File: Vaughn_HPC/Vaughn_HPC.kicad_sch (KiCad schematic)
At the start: 24 parts, among them U1 LM7805_TO220, U2 LM7812_TO220

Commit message: WIP
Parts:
- added J1: Conn_01x06_Pin, symbol Connector:Conn_01x06_Pin
- added R1, R2, R3, R4, R5, R6: R, symbol Device:R
- added R7: 1M, symbol Device:R
- added R8, R9: 1K, symbol Device:R
- added U3: PIC16LF1938-I/SP, SPDIP28_300MC_MCH, symbol PIC16LF1933:PIC16LF1938-I_SP
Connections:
- net at TR1.1: now also RV1.1
- net at TR1.4: now also RV1.2
- net at TR1.5: now also D3.2 (A), D4.1 (K), TR1.7
- net at TR1.6: now also D1.1 (K), D2.2 (A), TR1.8
- net at C2.1: now also U2.3 (VO)
- net GND: now reaches C2.2
- net GND: now also C1.2, C3.2, C4.2, D1.2 (A), D4.2 (A), U1.2 (GND), U2.2 (GND), R1.2, R2.2, R3.2, R4.1, R5.2, R6.1, U3.19 (VSS), U3.8 (VSS)
- net at U1.3 (VO): now also C3.1
- net at C1.1: now also D2.1 (K), D3.1 (K)
- net at C4.1: now also U3.20 (VDD)
- new net: R3.1, U3.2 (RA0)
- new net: R4.2, U3.3 (RA1)
- new net: R2.1, U3.5 (RA3)
- new net: R1.1, U3.21 (RB0)
- new net: R9.1, U3.12 (RC1)
- new net: R5.1, U3.24 (RB3)
- new net: R6.2, U3.4 (RA2), U3.7 (RA5)
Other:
- moved on the sheet: C1, C2, C3, C4, D1, D2, D3, D4, RN1, RN2, TP1, TP10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

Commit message: Add files via upload
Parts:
- removed TP1, TP10, TP2, TP3, TP4, TP5, TP6, TP7, TP8, TP9: TestPoint, symbol Connector:TestPoint
- added D5, D6, D7, D9: 1N4001, Diode_THT:D_DO-41_SOD81_P10.16mm_Horizontal, symbol Diode:1N4001
- added J2, J3, J4: AZ943-1CH-24DE, AZ9431CH24DE, symbol sugar:AZ943-1CH-24DE
- added K1: AZ2100-1A-12DEF, AZ21001A12DEF, symbol cubey:AZ2100-1A-12DEF
- added Q1, Q2, Q3, Q5: 2N3904, Package_TO_SOT_THT:TO-92_Inline, symbol Transistor_BJT:2N3904
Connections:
- net at C2.1, U2.3 (VO): now also U1.1 (VI)
- net at U2.1 (VI): now also C1.1, D2.1 (K), D3.1 (K)
- new net: D9.1 (K), K1.3 (COIL_2)
- new net: D9.2 (A), K1.2 (COIL_1)
- new net: D6.2 (A), J3.2 (COIL_1)
- new net: D6.1 (K), J3.5 (COIL_2)
- new net: D5.2 (A), J2.2 (COIL_1)
- new net: D5.1 (K), J2.5 (COIL_2)
- new net: D7.2 (A), J4.2 (COIL_1)
- new net: D7.1 (K), J4.5 (COIL_2)
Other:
- moved on the sheet: C1, C2, C3, J1, U1, U2

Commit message: Add files via upload
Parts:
- added J10, J11, J12, J13, J14, J15, J16, J17, J5, J8, J9: 1287, 1287:KEYSTONE_1287, symbol spade2:1287
- added J6, J7: 1267, 1267:KEYSTONE_1267, symbol spade:1267
- renumbered Q5 to Q4
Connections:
- net GND: now also Q1.1 (E), Q2.1 (E), Q3.1 (E), Q4.1 (E)
- net at RV1.1, TR1.1: now also J16.1_1
- net at RV1.2, TR1.4: now also J17.1_2
- net at J3.1 (COM): now also J11.1_2
- net at J3.3 (NO): now also J12.1_1
- net at J3.4 (NC): now also J10.1_2
- net 12V: now reaches D6.1 (K), J3.5 (COIL_2)
- net 12V: now also C2.1, D5.1 (K), D7.1 (K), J2.5 (COIL_2), J4.5 (COIL_2), U1.1 (VI), U2.3 (VO)
- net at J2.1 (COM): now also J8.1_2
- net at J2.3 (NO): now also J9.1_1
- net at J2.4 (NC): now also J5.1_2
- net 5V: now reaches C3.1, U1.3 (VO)
- net at J4.1 (COM): now also J13.1_2
- net at J4.3 (NO): now also J15.1_1
- net at J4.4 (NC): now also J14.1_2
- net at K1.1 (COM): now also J6.1
- net at K1.4 (NO): now also J7.1
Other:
- moved on the sheet: C1, C2, C3, C4, D1, D2, D3, D4, D5, D6, D7, D9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

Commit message: Update Vaughn_HPC.kicad_sch
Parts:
- R9: value 1K -> 120
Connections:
- net GND: now also J1.4 (Pin_4)
- net at D6.2 (A), J3.2 (COIL_1): now also Q2.3 (C)
- net at Q3.3 (C): now also D7.2 (A), J4.2 (COIL_1)
- net at D5.2 (A), J2.2 (COIL_1): now also Q1.3 (C)
- net prog_p2: now reaches J1.2 (Pin_2)
- net prog_p2: now also U3.27 (RB6/ICSPCLK/ICDCLK)
- net at J1.5 (Pin_5): now also R7.1
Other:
- moved on the sheet: Q1, Q2, Q3, R7

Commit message: updated Traces
Bom
not done, but very close.
missing a couple connectors, and the specific mosfets
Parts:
- added J12, J13, J14, J15, J16: 1825640000, CONN4_1825640000_WED, symbol quickConnect:1825640000
- renumbered Q4 to Q1, Q1 to Q4
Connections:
- net GND: now also J16.4; no longer Q1.1 (E)
- net RP2_3_q1_Emitter: now reaches RN2.3 (R2)
- net RP2_3_q1_Emitter: now also Q1.1 (E)
- net at D9.2 (A), K1.2 (COIL_1): now also Q1.3 (C)
- net RP1_4_q3_base: now reaches Q3.2 (B)
- net RP1_4_q3_base: now also RN1.4 (R3)
- net RP1_6_q4_base: now reaches Q4.2 (B)
- net RP1_6_q4_base: now also RN1.6 (R5)
- net prog1_j14: now reaches J1.1 (Pin_1)
- net prog1_j14: now also J14.1
- net prog3_mcu28: now reaches J1.3 (Pin_3)
- net prog3_mcu28: now also U3.28 (RB7/ICSPDAT/ICDDAT)
- net prog6_mcu1: now reaches J1.6 (Pin_6)
- net prog6_mcu1: now also U3.1 (VPP/*MCLR/RE3)
- net mcu11_j16: now reaches U3.11 (RC0)
- net mcu11_j16: now also J16.1
- net RP1_1_mcu6: now reaches U3.6 (RA4)
- net mcu9_array1: now reaches U3.9 (RA7)
- net mcu9_array1: now also RN1.1 (common)
- net RP1_2_Q2_base: now reaches Q2.2 (B)
- net RP1_2_Q2_base: now also RN1.2 (R1)
- net RP1_8_q1_base: now reaches RN1.8 (R7)
- net prog_p2 renamed prog2_mcu27
- new net: J12.1, J13.4, J14.4, J15.4
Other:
- moved on the sheet: Q1

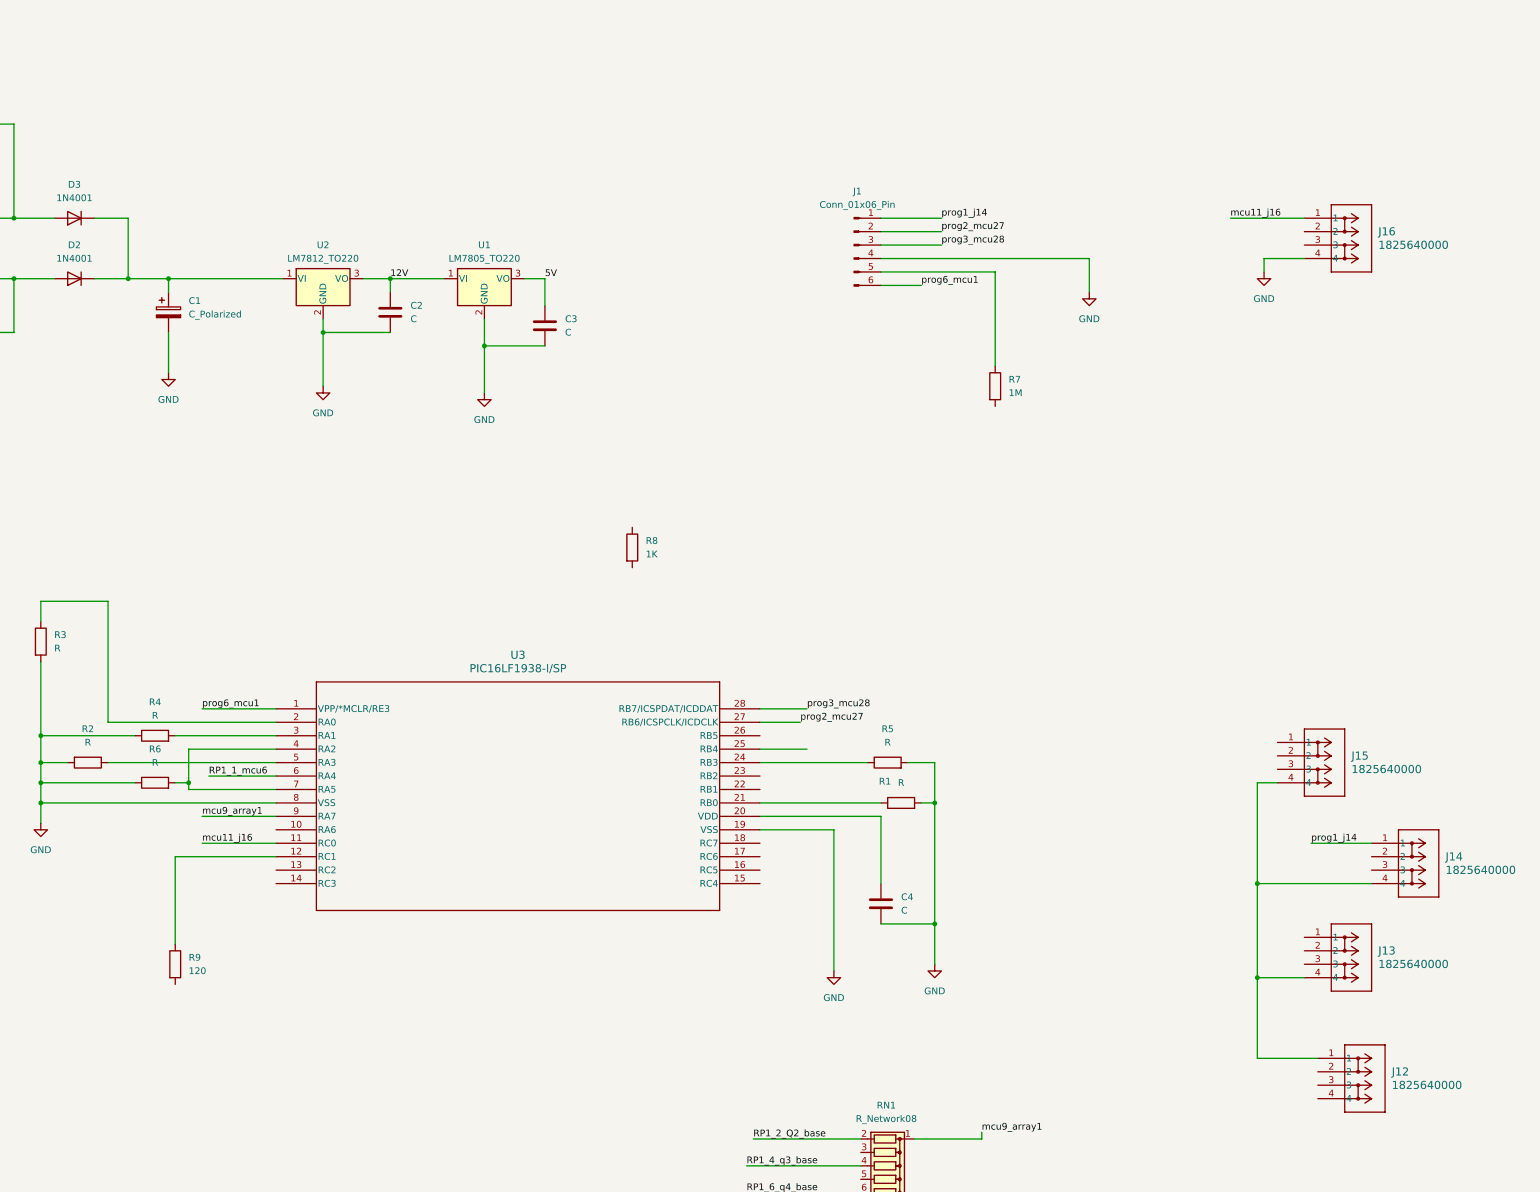
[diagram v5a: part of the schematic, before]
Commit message: add the LED
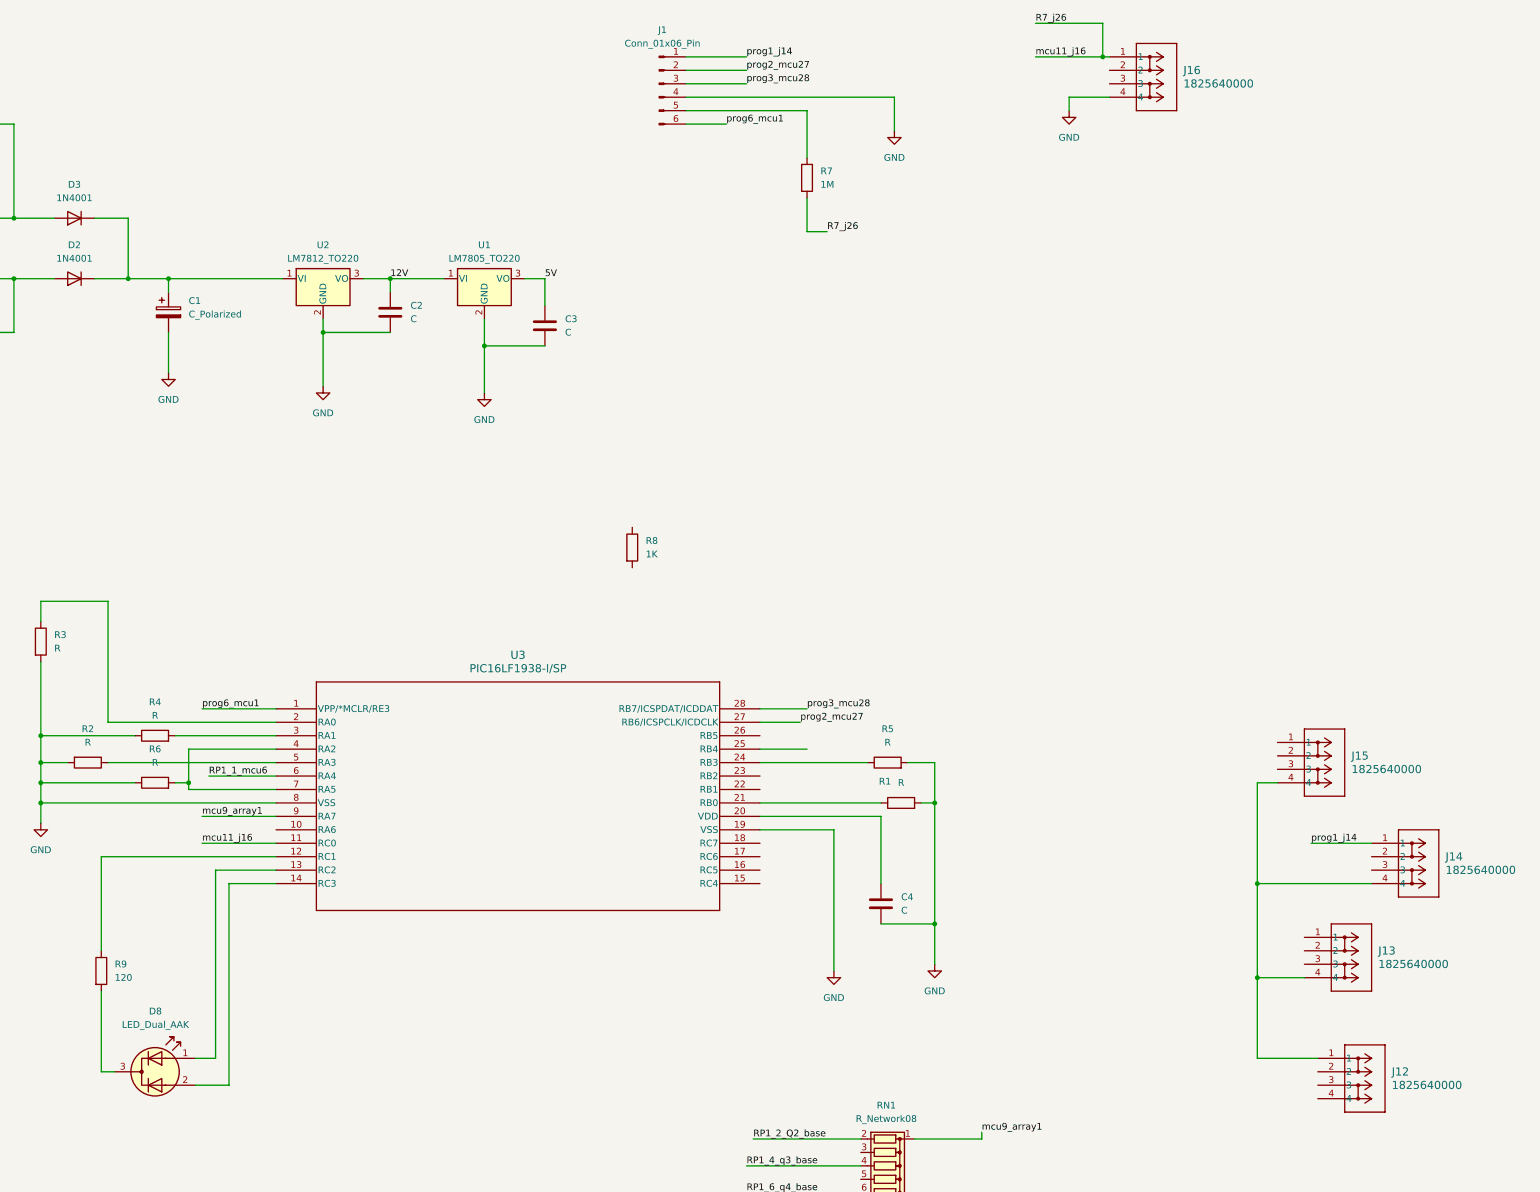
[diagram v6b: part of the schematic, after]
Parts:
- added D8: LED_Dual_AAK, symbol Device:LED_Dual_AAK
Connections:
- net mcu11_j16 is gone; now on net R7_j26: J16.1, U3.11 (RC0)
- net at R9.2: now also D8.3 (K)
- net at U3.13 (RC2): now also D8.1 (A1)
- net at U3.14 (RC3): now also D8.2 (A2)
- net R7_j26: now reaches R7.2
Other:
- moved on the sheet: J1, J16, R7, R9

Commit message: add generic mosfets
The current mosfet inclusion is not specificly correct. the circuit is a handwaving, sort of operation. JP4 is some 5 pin jst plug I dont want to hunt down right now. the order, and relative connections are fine, its just not a screw terminal.

The Mosfets are from international relay, but the datasheet doesnt lable the pins. I think it might got G-D-S but im not certain.
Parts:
- added JP4: Screw_Terminal_01x05, symbol Connector:Screw_Terminal_01x05
- added Q5, Q6, Q7, Q8: BF244A, Package_TO_SOT_THT:TO-92_Inline, symbol Transistor_FET:BF244A
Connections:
- net GND: now also Q5.3 (S), Q6.3 (S), Q7.3 (S), Q8.3 (S)
- net mcu22_q8_gate: now reaches U3.22 (RB1)
- net mcu22_q8_gate: now also Q8.2 (G)
- net mcu23_q7_gate: now reaches U3.23 (RB2)
- net mcu23_q7_gate: now also Q7.2 (G)
- new net 12v: JP4.1 (Pin_1)
- new net q5_src: JP4.2 (Pin_2), Q5.1 (D)
- new net q6_src: JP4.3 (Pin_3), Q6.1 (D)
- new net q7_src: JP4.4 (Pin_4), Q7.1 (D)
- new net q8_src: JP4.5 (Pin_5), Q8.1 (D)

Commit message: traced more out
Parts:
- added JP2: Screw_Terminal_01x03, symbol Connector:Screw_Terminal_01x03
- added R11: 1K, symbol Device:R
- renumbered RN1 to RP1, RN2 to RP2
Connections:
- net GND: now also JP2.1 (Pin_1)
- net RP1_7_mcu10: now reaches U3.10 (RA6)
- net RP1_7_mcu10: now also RP1.7 (R6)
- net RP1_3_mcu15: now reaches U3.15 (RC4)
- net RP1_3_mcu15: now also RP1.3 (R2)
- net RP1_5_mcu16: now reaches U3.16 (RC5)
- net RP1_5_mcu16: now also RP1.5 (R4)
- net mcu17_JP2_2: now reaches U3.17 (RC6)
- net mcu17_JP2_2: now also JP2.2 (Pin_2)
- net mcu18_R11: now reaches U3.18 (RC7)
- net mcu18_R11: now also R11.1
- net mcu25_q6_gate: now reaches U3.25 (RB4)
- net mcu25_q6_gate: now also Q6.2 (G)
- net mcu26_q5_gate: now reaches U3.26 (RB5)
- net mcu26_q5_gate: now also Q5.2 (G)
- new net: JP2.3 (Pin_3), R11.2
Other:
- moved on the sheet: JP4
